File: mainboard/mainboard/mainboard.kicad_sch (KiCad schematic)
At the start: 7 parts

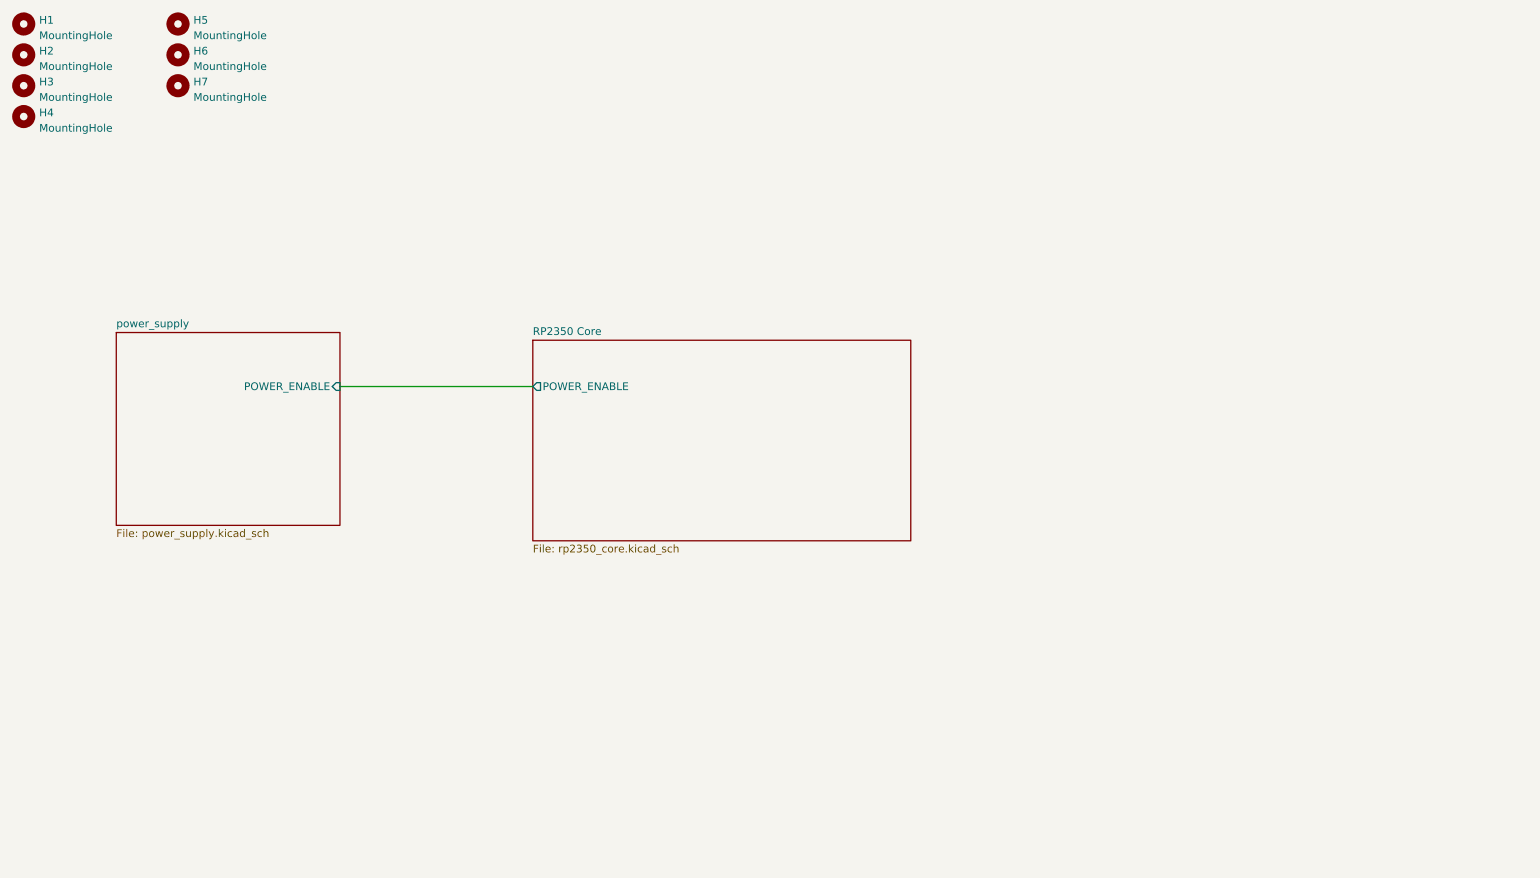
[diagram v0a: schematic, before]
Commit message: Share KiCad libraries, update v2.5 mainboard schematics
- Move every board's symbols, footprints and 3D models into libs/ and point
  the projects' lib tables there; add the mspc design-block library.
- Mainboard: new debug probe, MSPC bus and power connector sheets; drop the
  old shared-bus, south/north bridge and SD card sheets.
- Remove orphaned sheets from the GPU cards and the simulation sandbox.
- Rewrite the v2.5 plan, document libs/ in the README, ignore KiCad 10
  restore backups.

Co-Authored-By: Claude Opus 5 (1M context) <noreply@anthropic.com>
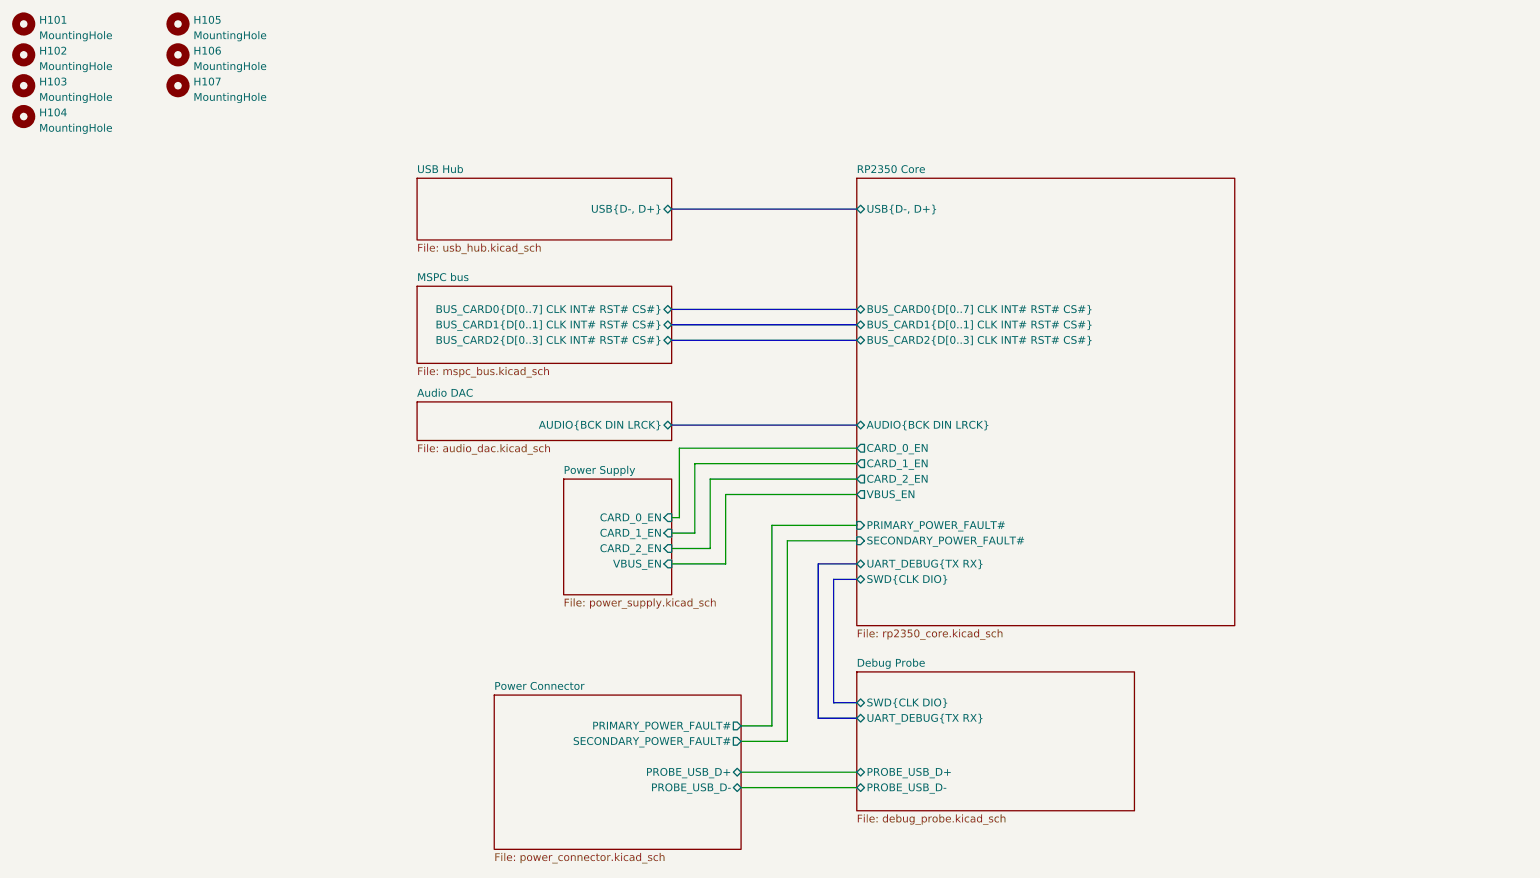
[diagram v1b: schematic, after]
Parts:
- renumbered H1 to H101, H2 to H102, H3 to H103, H4 to H104, H5 to H105, H6 to H106, H7 to H107
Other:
- sheet power_supply renamed Power Supply
- added sheet Audio DAC (audio_dac.kicad_sch)
- added sheet Debug Probe (debug_probe.kicad_sch)
- added sheet MSPC bus (mspc_bus.kicad_sch)
- added sheet Power Connector (power_connector.kicad_sch)
- added sheet USB Hub (usb_hub.kicad_sch)
- sheet Power Supply ports: added CARD_0_EN, CARD_1_EN, CARD_2_EN, VBUS_EN; removed POWER_ENABLE
- sheet RP2350 Core ports: added AUDIO{BCK DIN LRCK}, BUS_CARD0{D[0..7] CLK INT# RST# CS#}, BUS_CARD1{D[0..1] CLK INT# RST# CS#}, BUS_CARD2{D[0..3] CLK INT# RST# CS#}, CARD_0_EN, CARD_1_EN, CARD_2_EN, PRIMARY_POWER_FAULT#, SECONDARY_POWER_FAULT#, SWD{CLK DIO}, UART_DEBUG{TX RX}, USB{D-, D+}, VBUS_EN; removed POWER_ENABLE

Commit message: Mainboard v3: schematic review fixes
New sheets for the housekeeping bus: TCA6408A expander, INA226/INA3221
power measurement and the MCP7940N RTC with a CR1220 backup cell.

Correctness:
- RTC load caps C241/C242 are 6.8 pF C0G 0402 (were a relay footprint).
- L50 is the AOTA-B201610S3R3-101-T with pin 1 on +1V1_MCU; U52 is an
  APS1604M-3SQR-SN on a 150-mil SOP-8.
- I2S is DIN=GPIO13, BCK=GPIO14, LRCK=GPIO15, as pico-extras audio_i2s
  expects. Expander INT# goes to GPIO42.
- ADC_AVDD filter (FB50, C74, C75), 33 ohm on SDIO CLK, SD ESD (U53/U54),
  PSRAM 1 uF, POWER_BUTTON 10 k pull-up, 10 uF at the SY6280 inputs.
- J_DBG: USBLC6-4SC6 on the probe USB, 47 uF polymer on +5V_DBG against
  charger overvoltage spikes, and bleeders on both USB-C VBUS inputs and
  on +5V_DBG.
- Power symbols point at their matching project_power symbols.

Parts and fields:
- Part numbers and LCSC codes for the purchased parts: push-push microSD
  J53, HRO USB-C J1/J2, stacked USB-A J90/J91, TLV70033DDCR, and others.
- Voltage, dielectric and tolerance fields on every capacitor and a
  tolerance on every resistor; the field is named "LCSC" everywhere.
- Hand-solder footprint variants where KiCad has one.

Drawing:
- References renumbered into the per-sheet ranges.
- Net names on the USB, crystal, DAC, CC and ISET nets; netclass
  patterns updated.
- No four-way junctions left.
- Notes for the slot pin 1 marking, J120 and firmware bring-up.

ERC is clean with all rules enabled.

Co-Authored-By: Claude Opus 5 (1M context) <noreply@anthropic.com>
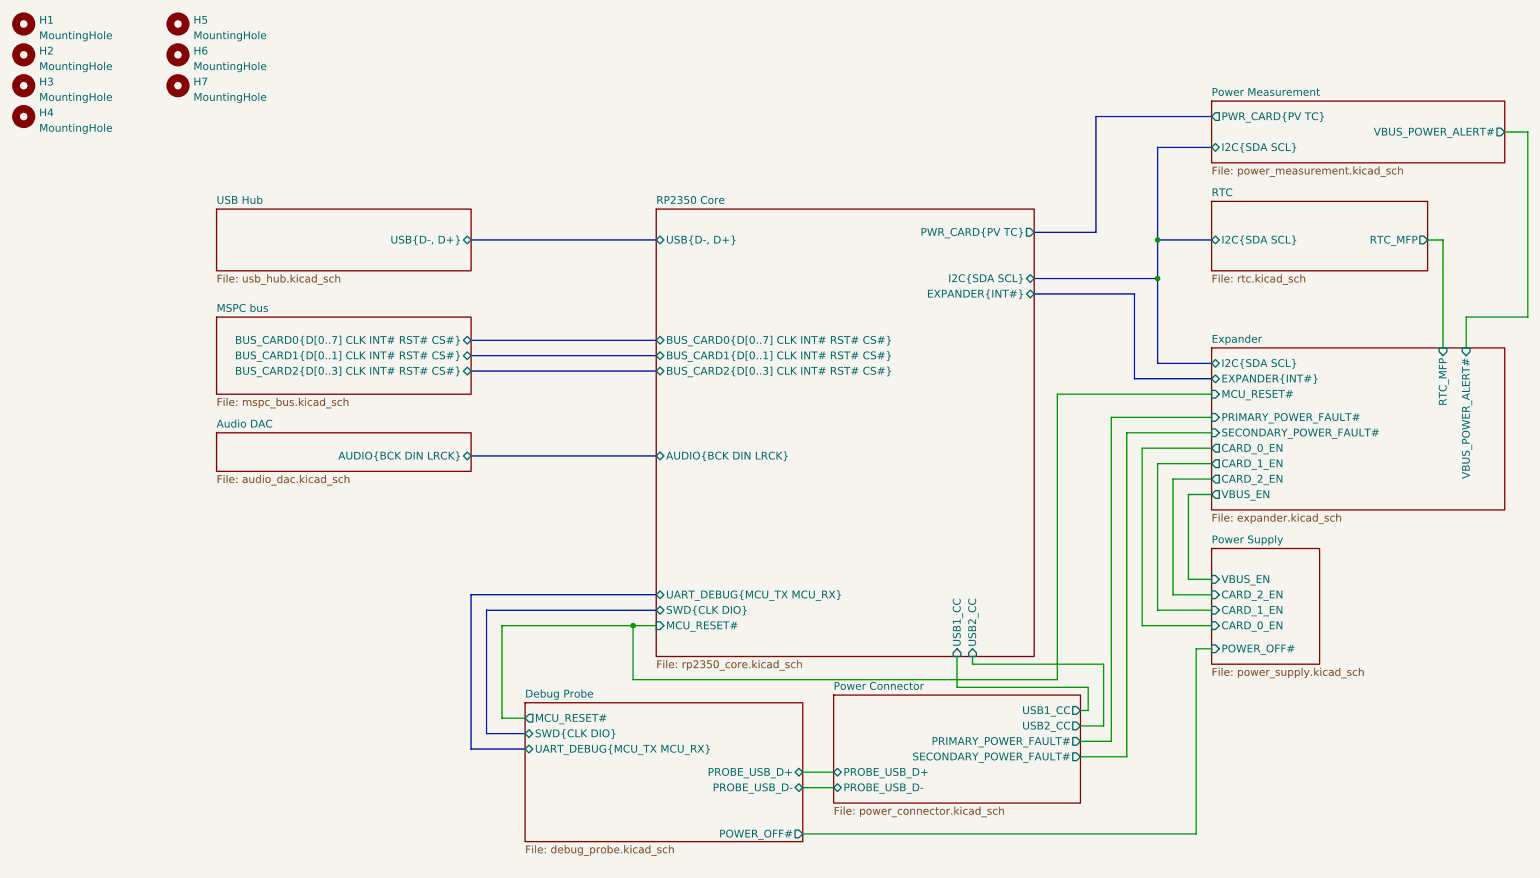
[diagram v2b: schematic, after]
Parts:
- renumbered H101 to H1, H102 to H2, H103 to H3, H104 to H4, H105 to H5, H106 to H6, H107 to H7
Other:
- added sheet Expander (expander.kicad_sch)
- added sheet Power Measurement (power_measurement.kicad_sch)
- added sheet RTC (rtc.kicad_sch)
- sheet Debug Probe ports: added MCU_RESET#, POWER_OFF#, UART_DEBUG{MCU_TX MCU_RX}; removed UART_DEBUG{TX RX}
- sheet Power Connector ports: added USB1_CC, USB2_CC; removed none
- sheet Power Supply ports: added POWER_OFF#; removed none
- sheet RP2350 Core ports: added EXPANDER{INT#}, I2C{SDA SCL}, MCU_RESET#, PWR_CARD{PV TC}, UART_DEBUG{MCU_TX MCU_RX}, USB1_CC, USB2_CC; removed CARD_0_EN, CARD_1_EN, CARD_2_EN, PRIMARY_POWER_FAULT#, SECONDARY_POWER_FAULT#, UART_DEBUG{TX RX}, VBUS_EN
